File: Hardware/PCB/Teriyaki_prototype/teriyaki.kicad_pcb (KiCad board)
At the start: 4 copper layers, 60 x 45 mm, 56 parts, among them J1 USB_B_Micro, J2 Conn_01x02, J3 Conn_01x10, J4 Conn_01x02, U1 XL1509, U2 STM8S105K6, U3 FT232RL, U4 USBLC6-2SC6, Y1 16MHz

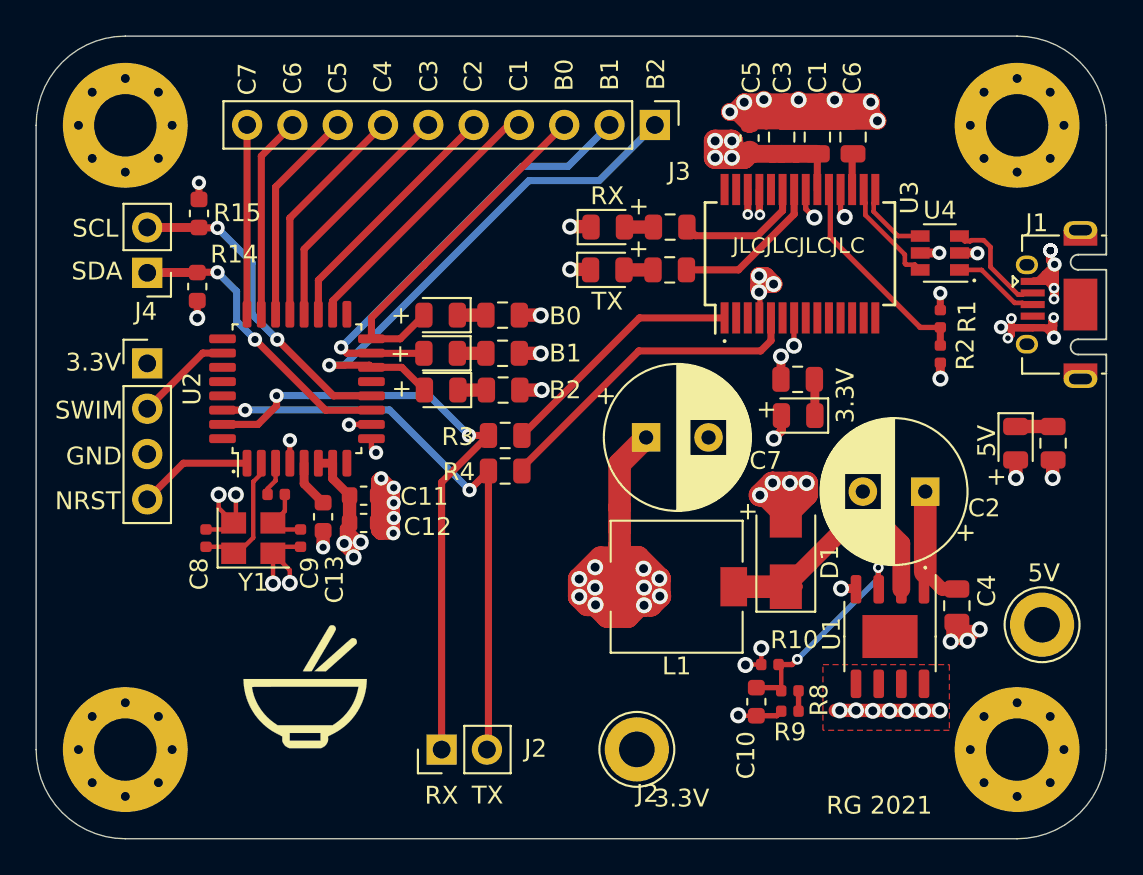
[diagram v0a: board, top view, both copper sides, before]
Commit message: update README and Teriyaki PCB Files
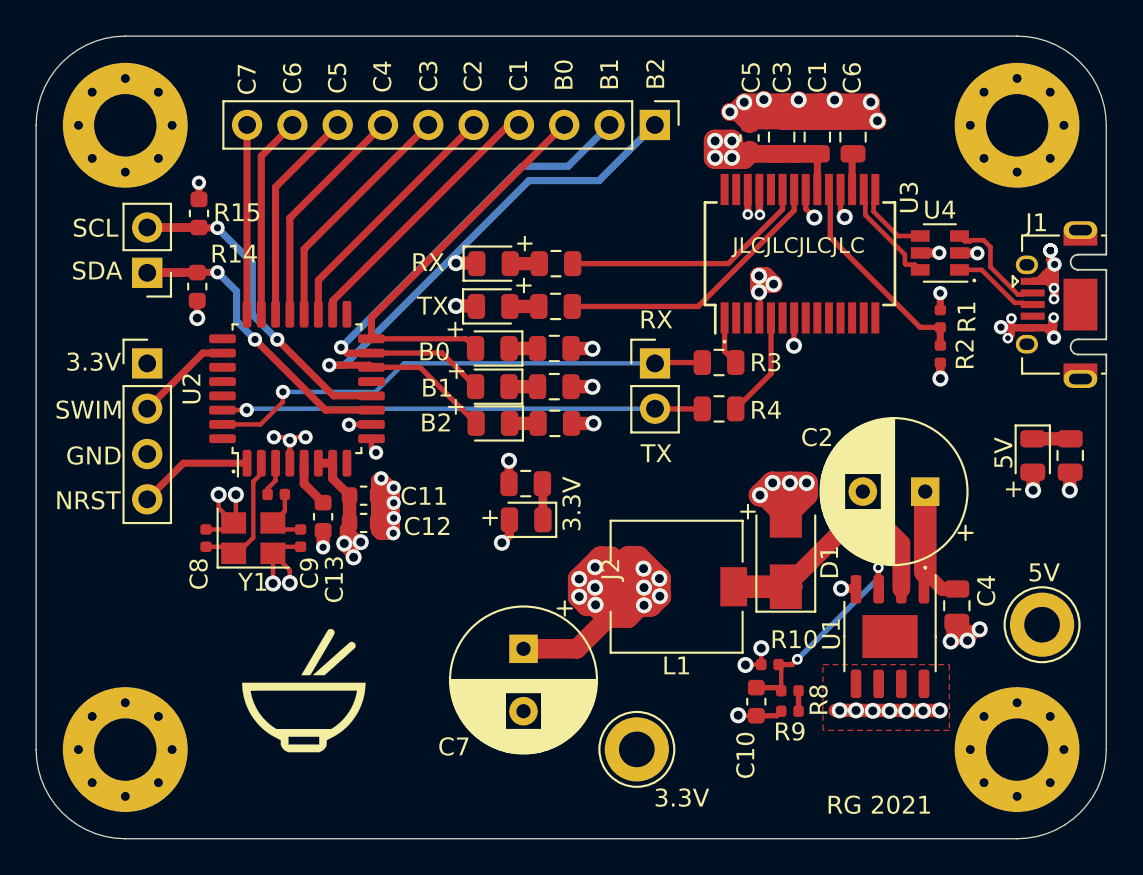
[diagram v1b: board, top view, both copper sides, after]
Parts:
- moved J2 24.7 mm to (121.7, 103.0), turned to 0 degrees
- moved R16 16.3 mm to (114.4, 109.8)
- moved LED_3V31 16.3 mm to (114.5, 111.8)
- moved C7 13.7 mm to (114.3, 119.0), turned to 270 degrees
- moved R3 12.7 mm to (125.3, 103.0)
- moved R4 12.5 mm to (125.3, 105.6)
- moved LED_RX1 6.72 mm to (112.6, 99.9)
- moved LED_TX1 6.72 mm to (112.6, 97.5)
- moved R5 6.72 mm to (116.1, 97.5)
- moved R6 6.72 mm to (116.1, 99.9)
- moved LED1 3.45 mm to (112.6, 106.4)
- moved LED2 3.45 mm to (112.6, 104.4)
- moved LED3 3.45 mm to (112.6, 102.2)
- moved R11 3.45 mm to (116.1, 104.4)
- moved R13 3.45 mm to (116.1, 102.2)
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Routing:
- net Net-(R4-Pad2): track 18.4 -> 5.92 mm
- net Net-(R3-Pad2): track 14.1 -> 2.76 mm
- net CBUS1: track 8.72 -> 15.8 mm
- net STM8_RX: track 35.6 -> 28.7 mm, vias 2 -> 1
- net CBUS0: track 7.33 -> 14.1 mm
- net STM8_TX: track 32.9 -> 27.0 mm, vias 2 -> 1
- net GPIO_B2: track 29.8 -> 33.4 mm
- net GPIO_B1: track 25.0 -> 28.7 mm
- net GPIO_B0: track 20.0 -> 22.5 mm
- net +3V3: track 74.8 -> 72.5 mm
- net GND: track 114.7 -> 116.6 mm, vias 55 -> 57
